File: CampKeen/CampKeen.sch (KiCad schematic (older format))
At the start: 192 parts, among them IC1 LM2597MX-ADJ_NOPB, IC2 LM2670SX-5.0_NOPB, IC3 DS3231SN#, IC4 TL071CP, J1 Vin, J2 CAC, J3 VAC, J4 Screw_Terminal_01x04, J5 GenEnclosure, J6 GenHeadL, J7 GenHeadR, K1 DIP05-1A72-12L, K2 DIP05-1A72-12L, K3 DIP05-1A72-12L, K4 DIP05-1A72-12L, P1 Power, P10 CONN_01X01, P11 CONN_01X01, P12 CONN_01X01, P13 CONN_01X01, P2 Analog, P3 Analog, P4 Digital, P5 PWM, P6 PWM, P7 Communication, P8 CONN_01X01, P9 CONN_01X01, Q1 BC547, Q10 2N7000, Q11 2N7000, Q12 2N7000, Q13 2N7000, Q14 2N7000, Q15 IRF510, Q16 2N7000, Q17 IRF510, Q18 2N7000, Q19 IRF510, Q2 2N7000, Q20 2N7000, Q21 IRF510, Q22 BC547, Q23 2N7000, Q24 IRF510, Q25 2N7000, Q26 2N7000, Q27 IRF510, Q28 2N7000, Q29 IRF510, Q3 2N7000, Q30 2N7000, Q31 IRF510, Q32 BC547, Q33 2N7000, Q35 2N7000, Q36 IRF510, Q37 2N7000, Q38 IRF510, Q39 IRF510, Q4 2N7000, Q40 IRF9Z34NPBF, Q5 2N7000, Q6 BC547, Q7 2N7000, Q8 2N7000, Q9 2N7000, T1 F24-045-C2, U2 MAX232

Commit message: working on the PCB for 0.3
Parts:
- removed IC4: TL071CP, SamacSys_Parts:DIP794W53P254L959H508Q8N, symbol SamacSys_Parts:TL071CP
- removed RV1: 500K, Potentiometer_THT:Potentiometer_Bourns_3296W_Vertical, symbol Device:R_POT_US
- added IC4: INA849DR, SamacSys_Parts:SOIC127P600X175-8N, symbol SamacSys_Parts:INA849DR
- added IC5: LM2904N_NOPB, SamacSys_Parts:DIP794W53P254L959H508Q8N, symbol SamacSys_Parts:LM2904N_NOPB
- added R82: 20K, Resistor_THT:R_Axial_DIN0207_L6.3mm_D2.5mm_P2.54mm_Vertical, symbol Device:R
- added U1: TL431LP, Package_TO_SOT_THT:TO-92_Inline, symbol Reference_Voltage:TL431LP
- R25: footprint Resistor_THT:R_Axial_DIN0207_L6.3mm_D2.5mm_P2.54mm_Vertical -> Resistor_THT:R_Axial_DIN0207_L6.3mm_D2.5mm_P10.16mm_Horizontal
- R29: value 100k -> 1K
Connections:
- net +5V: now also IC4.8 (+VS), IC5.8 (V+)
- net A0: now also IC5.6 (INVERTING_INPUT_B), IC5.7 (OUTPUT_B)
- net A12: now also IC4.7 (OUT); no longer C11.1, J2.2 (Pin_2), R25.1, R29.1, R90.2
- net GND: now also IC4.5 (-VS), IC5.4 (GND), R82.1, U1.2 (A); no longer C11.2
- net at R28.1: now also IC5.5 (NON-INVERTING_INPUT_B), R82.2
- net at T1.5 (12V_@_0.045A_1): now also BR1.3 (~_1); no longer BR1.4 (~_2)
- net at T1.6 (12V_@_0.045A_2): now also BR1.4 (~_2); no longer BR1.3 (~_1)
- net at J2.1 (Pin_1), R25.2: now also C11.1, IC4.1 (-IN)
- new net: IC5.3 (NON-INVERTING_INPUT_A), R29.1, U1.1 (REF), U1.3 (K)
- new net: C11.2, IC4.4 (+IN), J2.2 (Pin_2), R25.1
- new net: IC4.6 (REF), IC5.1 (OUTPUT_A), IC5.2 (INVERTING_INPUT_A), R90.2
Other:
- moved on the sheet: C11, J2, R25, R28, R29, R35, R90

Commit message: 0.3 fixing a bug found in 0.2 hardware.
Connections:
- net +5V: now also K1.2 (COIL_1), K2.2 (COIL_1); no longer Q1.1 (C), Q32.1 (C), Q6.1 (C)
- net GND: now also Q1.3 (E), Q32.3 (E), Q6.3 (E); no longer K1.6 (COIL_2), K2.6 (COIL_2)
- net at O1.11: now also Q32.1 (C); no longer Q32.3 (E)
- new net: K1.6 (COIL_2), Q1.1 (C)
- new net: K2.6 (COIL_2), Q6.1 (C)
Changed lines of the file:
@@
 L power:GND #PWR049
 U 1 1 612DE713
-P 15100 4300
-F 0 "#PWR049" H 15100 4050 50  0001 C CNN
-F 1 "GND" H 15105 4127 50  0000 C CNN
-F 2 "" H 15100 4300 50  0001 C CNN
-F 3 "" H 15100 4300 50  0001 C CNN
-	1    15100 4300
+P 16200 5850
+F 0 "#PWR049" H 16200 5600 50  0001 C CNN
+F 1 "GND" H 16205 5677 50  0000 C CNN
+F 2 "" H 16200 5850 50  0001 C CNN
+F 3 "" H 16200 5850 50  0001 C CNN
+	1    16200 5850
 	1    0    0    -1
 $EndComp
 Wire Wire Line
-	15350 4100 15100 4100
-Wire Wire Line
-	15100 4100 15100 4300
-Wire Wire Line
 	15350 4200 15350 4400
 Wire Wire Line
@@
 	1    0    0    -1
 $EndComp
-Wire Wire Line
-	8350 3950 8350 4050
-Wire Wire Line
-	8350 4050 8900 4050
-Wire Wire Line
-	8350 3550 8350 3300
 $Comp
 L power:+5V #PWR029
 U 1 1 621E716D
-P 8350 3300
-F 0 "#PWR029" H 8350 3150 50  0001 C CNN
-F 1 "+5V" H 8365 3473 50  0000 C CNN
-F 2 "" H 8350 3300 50  0001 C CNN
-F 3 "" H 8350 3300 50  0001 C CNN
-	1    8350 3300
+P 8800 3400
+F 0 "#PWR029" H 8800 3250 50  0001 C CNN
+F 1 "+5V" H 8815 3573 50  0000 C CNN
+F 2 "" H 8800 3400 50  0001 C CNN
+F 3 "" H 8800 3400 50  0001 C CNN
+	1    8800 3400
 	1    0    0    -1
 $EndComp
@@
 	0    1    1    0
 $EndComp
-Wire Wire Line
-	8900 4150 8650 4150
 $Comp
 L power:GND #PWR031
 U 1 1 61234D77
-P 8650 4350
-F 0 "#PWR031" H 8650 4100 50  0001 C CNN
-F 1 "GND" H 8655 4177 50  0000 C CNN
-F 2 "" H 8650 4350 50  0001 C CNN
-F 3 "" H 8650 4350 50  0001 C CNN
-	1    8650 4350
+P 8350 4150
+F 0 "#PWR031" H 8350 3900 50  0001 C CNN
+F 1 "GND" H 8355 3977 50  0000 C CNN
+F 2 "" H 8350 4150 50  0001 C CNN
+F 3 "" H 8350 4150 50  0001 C CNN
+	1    8350 4150
 	1    0    0    -1
 $EndComp
@@
 	0    1    1    0
 $EndComp
-$Comp
-L power:+5V #PWR051
-U 1 1 6236099A
-P 15850 5100
-F 0 "#PWR051" H 15850 4950 50  0001 C CNN
-F 1 "+5V" H 15865 5273 50  0000 C CNN
-F 2 "" H 15850 5100 50  0001 C CNN
-F 3 "" H 15850 5100 50  0001 C CNN
-	1    15850 5100
-	1    0    0    -1
-$EndComp
-Wire Wire Line
-	15850 5350 15850 5100
 Wire Wire Line
 	15850 5750 15850 5850
@@
 Wire Wire Line
 	15850 5850 16200 5850
-Wire Wire Line
-	16200 5850 16200 4700
-Wire Wire Line
-	16200 4700 15200 4700
-Wire Wire Line
-	15200 4700 15200 4000
-Wire Wire Line
-	15200 4000 15350 4000
 $Comp
 L Transistor_FET:2N7000 Q2
@@
 Wire Wire Line
 	20100 22750 20250 22750
-Wire Wire Line
-	8650 4150 8650 4350
 $Comp
 L power:GND #PWR028
@@
 	32400 9000 32400 8000
 Wire Wire Line
-	36350 9000 32400 9000
-Wire Wire Line
-	36350 10500 36350 9000
-Wire Wire Line
 	32300 8100 32150 8100
 Wire Wire Line
@@
 LCDBacklightOut
 Wire Wire Line
-	35500 10500 36350 10500
-Wire Wire Line
 	35500 10000 35500 10500
 Wire Wire Line
@@
 $EndComp
 $Comp
-L power:+5V #PWR0130
-U 1 1 6262263F
-P 35500 9350
-F 0 "#PWR0130" H 35500 9200 50  0001 C CNN
-F 1 "+5V" H 35515 9523 50  0000 C CNN
-F 2 "" H 35500 9350 50  0001 C CNN
-F 3 "" H 35500 9350 50  0001 C CNN
-	1    35500 9350
-	1    0    0    -1
-$EndComp
-Wire Wire Line
-	35500 9600 35500 9350
-$Comp
 L Transistor_BJT:BC547 Q32
 U 1 1 62622636
@@
 Wire Wire Line
 	19500 23700 20050 23700
+Connection ~ 20050 23700
+Wire Wire Line
+	20050 23700 20050 23650
+Wire Wire Line
+	8350 4150 8350 3950
+Wire Wire Line
+	8350 3550 8550 3550
+Wire Wire Line
+	8550 3550 8550 4150
+Wire Wire Line
+	8550 4150 8900 4150
+Wire Wire Line
+	8900 4050 8800 4050
+Wire Wire Line
+	8800 3400 8800 4050
+$Comp
+L power:+5V #PWR051
+U 1 1 6236099A
+P 15150 3750
+F 0 "#PWR051" H 15150 3600 50  0001 C CNN
+F 1 "+5V" H 15165 3923 50  0000 C CNN
+F 2 "" H 15150 3750 50  0001 C CNN
+F 3 "" H 15150 3750 50  0001 C CNN
+	1    15150 3750
+	1    0    0    -1
+$EndComp
+Wire Wire Line
+	15150 4000 15150 3750
+Wire Wire Line
+	15150 4000 15350 4000
+Wire Wire Line
+	15850 5350 15850 4700
+Wire Wire Line
+	15850 4700 15150 4700
+Wire Wire Line
+	15150 4700 15150 4100
+Wire Wire Line
+	15150 4100 15350 4100
+$Comp
+L power:GND #PWR?
+U 1 1 62559C03
+P 35500 10500
+F 0 "#PWR?" H 35500 10250 50  0001 C CNN
+F 1 "GND" H 35505 10327 50  0000 C CNN
+F 2 "" H 35500 10500 50  0001 C CNN
+F 3 "" H 35500 10500 50  0001 C CNN
+	1    35500 10500
+	1    0    0    -1
+$EndComp
+Wire Wire Line
+	35500 9600 35500 9000
+Wire Wire Line
+	35500 9000 32400 9000
 Wire Bus Line
 	8600 7000 25650 7000
@@
 Wire Bus Line
 	21850 16650 25650 16650
-Connection ~ 20050 23700
-Wire Wire Line
-	20050 23700 20050 23650
 $EndSCHEMATC

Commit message: before removing my homegrown AC monitoring stuff.
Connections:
- net +5V: now also K4.2 (COIL_1); no longer Q22.1 (C)
- net GND: now also Q22.3 (E); no longer K4.6 (COIL_2)
- new net: K4.6 (COIL_2), Q22.1 (C)
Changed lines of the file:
@@
 	1    0    0    -1
 $EndComp
-Wire Wire Line
-	30500 16950 30500 17050
-Wire Wire Line
-	30500 17050 31050 17050
-Wire Wire Line
-	30500 16550 30500 16300
 $Comp
 L power:+5V #PWR0110
 U 1 1 621F0FD9
-P 30500 16300
-F 0 "#PWR0110" H 30500 16150 50  0001 C CNN
-F 1 "+5V" H 30515 16473 50  0000 C CNN
-F 2 "" H 30500 16300 50  0001 C CNN
-F 3 "" H 30500 16300 50  0001 C CNN
-	1    30500 16300
+P 30850 16350
+F 0 "#PWR0110" H 30850 16200 50  0001 C CNN
+F 1 "+5V" H 30865 16523 50  0000 C CNN
+F 2 "" H 30850 16350 50  0001 C CNN
+F 3 "" H 30850 16350 50  0001 C CNN
+	1    30850 16350
 	1    0    0    -1
 $EndComp
@@
 	0    1    1    0
 $EndComp
-Wire Wire Line
-	31050 17150 30800 17150
 $Comp
 L power:GND #PWR0115
 U 1 1 621F0FE6
-P 30800 17350
-F 0 "#PWR0115" H 30800 17100 50  0001 C CNN
-F 1 "GND" H 30805 17177 50  0000 C CNN
-F 2 "" H 30800 17350 50  0001 C CNN
-F 3 "" H 30800 17350 50  0001 C CNN
-	1    30800 17350
+P 30500 17250
+F 0 "#PWR0115" H 30500 17000 50  0001 C CNN
+F 1 "GND" H 30505 17077 50  0000 C CNN
+F 2 "" H 30500 17250 50  0001 C CNN
+F 3 "" H 30500 17250 50  0001 C CNN
+	1    30500 17250
 	1    0    0    -1
 $EndComp
-Wire Wire Line
-	30800 17150 30800 17350
 $Comp
 L power:GND #PWR0109
@@
 	12100 14800 12100 14700
 Connection ~ 12100 14600
-Connection ~ 12100 14800
 Wire Wire Line
 	12600 14700 12100 14700
@@
 	12100 14700 12100 14600
 Wire Wire Line
-	12600 14900 12100 14900
-Wire Wire Line
-	12100 14900 12100 14800
-Wire Wire Line
 	13900 15100 13500 15100
 Wire Wire Line
@@
 	15150 4100 15350 4100
 $Comp
-L power:GND #PWR?
+L power:GND #PWR0130
 U 1 1 62559C03
 P 35500 10500
-F 0 "#PWR?" H 35500 10250 50  0001 C CNN
+F 0 "#PWR0130" H 35500 10250 50  0001 C CNN
 F 1 "GND" H 35505 10327 50  0000 C CNN
 F 2 "" H 35500 10500 50  0001 C CNN
@@
 Wire Wire Line
 	35500 9000 32400 9000
+Wire Wire Line
+	30500 16950 30500 17250
+Wire Wire Line
+	31050 17050 30850 17050
+Wire Wire Line
+	30850 17050 30850 16350
+Wire Wire Line
+	30500 16550 30800 16550
+Wire Wire Line
+	30800 16550 30800 17150
+Wire Wire Line
+	30800 17150 31050 17150
 Wire Bus Line
-	8600 7000 25650 7000
+	25650 12850 40250 12850
+Wire Bus Line
+	25650 7000 42500 7000
 Wire Bus Line
 	36400 16150 36400 18600
@@
 	21650 18600 36400 18600
 Wire Bus Line
-	25650 7000 42500 7000
-Wire Bus Line
-	25650 12850 40250 12850
-Wire Bus Line
 	25650 12850 25650 16650
 Wire Bus Line
 	21850 16650 25650 16650
+Wire Bus Line
+	8600 7000 25650 7000
+Connection ~ 12100 14800
+Wire Wire Line
+	12100 14900 12100 14800
+Wire Wire Line
+	12600 14900 12100 14900
 $EndSCHEMATC

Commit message: files submitted for Fab Verions 0.5
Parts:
- removed BR1: DF04M, SamacSys_Parts:DIP825W58P510L828H330Q4N, symbol SamacSys_Parts:DF04M
- removed C11: 10uF, Capacitor_THT:C_Rect_L9.0mm_W3.6mm_P7.50mm_MKT, symbol Device:C
- removed C12: 2.2uF, Capacitor_THT:CP_Radial_D4.0mm_P2.00mm, symbol Device:CP
- removed C13: 10nF, Capacitor_THT:C_Disc_D7.5mm_W5.0mm_P5.00mm, symbol Device:C
- removed IC4: INA849DR, SamacSys_Parts:SOIC127P600X175-8N, symbol SamacSys_Parts:INA849DR
- removed IC5: LM2904N_NOPB, SamacSys_Parts:DIP794W53P254L959H508Q8N, symbol SamacSys_Parts:LM2904N_NOPB
- removed J2: CAC, TerminalBlock_Phoenix:TerminalBlock_Phoenix_MKDS-1,5-2-5.08_1x02_P5.08mm_Horizontal, symbol Connector:Screw_Terminal_01x02
- removed K3: DIP05-1A72-12L, SamacSys_Parts:DIP051A7212L, symbol SamacSys_Parts:DIP05-1A72-12L
- removed R25: 33, Resistor_THT:R_Axial_DIN0207_L6.3mm_D2.5mm_P10.16mm_Horizontal, symbol Device:R
- removed R29: 1K, Resistor_THT:R_Axial_DIN0207_L6.3mm_D2.5mm_P2.54mm_Vertical, symbol Device:R
- removed R30: 1M, Resistor_THT:R_Axial_DIN0207_L6.3mm_D2.5mm_P2.54mm_Vertical, symbol Device:R
- removed R36: 180k, Resistor_THT:R_Axial_DIN0207_L6.3mm_D2.5mm_P2.54mm_Vertical, symbol Device:R
- removed R90: 100k, Resistor_THT:R_Axial_DIN0207_L6.3mm_D2.5mm_P2.54mm_Vertical, symbol Device:R
- removed T1: F24-045-C2, SamacSys_Parts:F24045C2, symbol SamacSys_Parts:F24-045-C2
- removed U1: TL431LP, Package_TO_SOT_THT:TO-92_Inline, symbol Reference_Voltage:TL431LP
- removed VACFuse1: VAC, SamacSys_Parts:BK_HTC-15M, symbol SamacSys_Parts:BK_HTC-15M
- added IC4: CD74HC4050ME4, SOIC127P600X175-16N, symbol SamacSys_Parts:CD74HC4050ME4
- added IC5: TL071CP, DIP794W53P254L959H508Q8N, symbol SamacSys_Parts:TL071CP
- added J2: CircuitSetupsSplitPhase, Connector_PinSocket_2.54mm:PinSocket_1x09_P2.54mm_Vertical, symbol Connector_Generic:Conn_01x09
- J3: value VAC -> Vin
- R2, R3: footprint Resistor_THT:R_Axial_DIN0207_L6.3mm_D2.5mm_P2.54mm_Vertical -> Resistor_THT:R_Axial_DIN0204_L3.6mm_D1.6mm_P7.62mm_Horizontal
- R82: value 20K -> 19.2K
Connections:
- net +12V: now also J3.1 (Pin_1)
- net +3V3: now also IC4.1 (VCC)
- net +5V: now also IC5.7 (VCC+)
- net 41: now also IC4.14 (6A); no longer Q35.1 (S), R83.1
- net 50(MISO): now also IC4.4 (2Y), IC4.5 (2A), J2.4 (Pin_4)
- net 51(MOSI): now also IC4.6 (3Y), IC4.7 (3A), J2.3 (Pin_3)
- net 52(SCK): now also IC4.3 (1A)
- net A0: now also IC5.2 (IN-), IC5.6 (OUT)
- net A11: no longer P3.4 (Pin_4)
- net A12: no longer P3.5 (Pin_5)
- net GND: now also J3.2 (Pin_2), IC4.8 (GND), IC5.4 (VCC-), J2.1 (Pin_1)
- net at R28.1, R82.2: now also IC5.3 (IN+)
- new net: Q35.1 (S), R83.1
- new net CS: IC4.15 (6Y), J2.6 (Pin_6)
- new net SCLK: IC4.2 (1Y), J2.5 (Pin_5)
- no-connect marks 36 -> 42
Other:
- moved on the sheet: C1, C10, C18, C2, C3, C4, C6, C7, C8, C9, D1, D2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

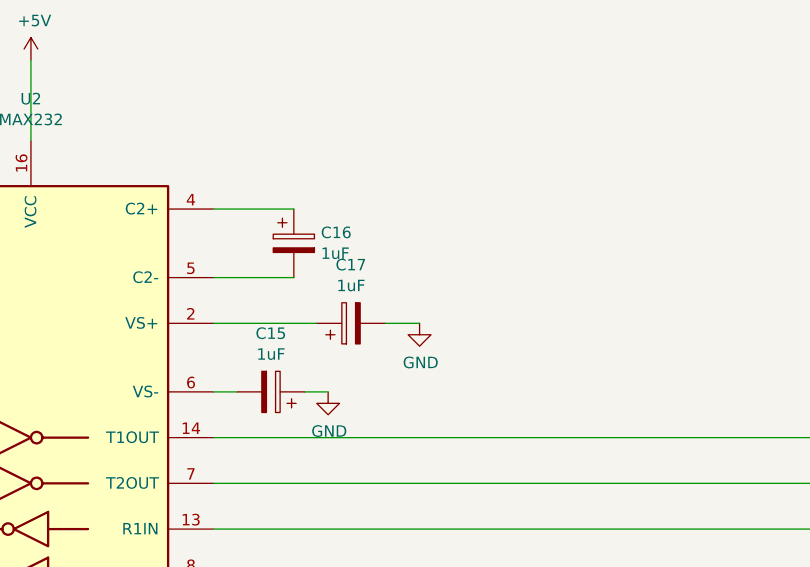
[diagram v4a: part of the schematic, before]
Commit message: fixed the mistake on the RS232 driver.
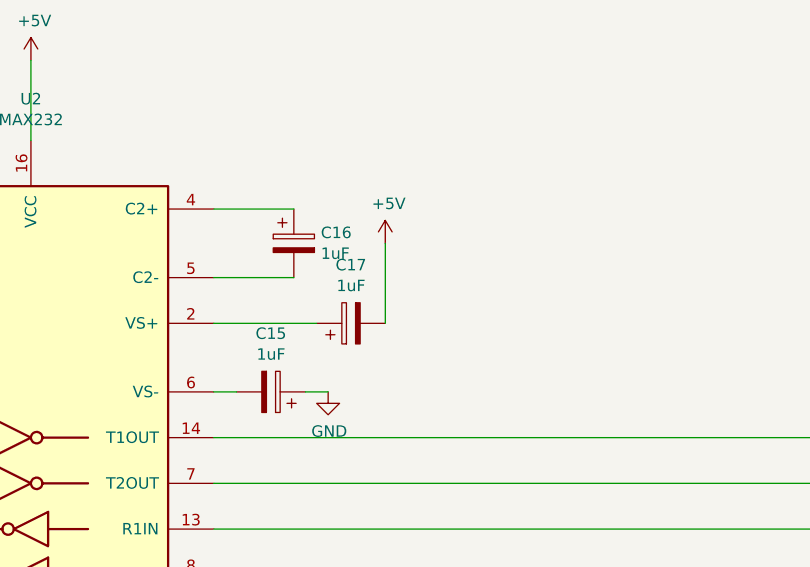
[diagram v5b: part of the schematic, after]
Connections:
- net +5V: now also C17.2
- net GND: no longer C17.2
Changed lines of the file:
@@
 	1    0    0    -1
 $EndComp
-$Comp
-L power:GND #PWR0108
-U 1 1 61FF6266
-P 29800 14900
-F 0 "#PWR0108" H 29800 14650 50  0001 C CNN
-F 1 "GND" H 29805 14727 50  0000 C CNN
-F 2 "" H 29800 14900 50  0001 C CNN
-F 3 "" H 29800 14900 50  0001 C CNN
-	1    29800 14900
-	1    0    0    -1
-$EndComp
 Wire Wire Line
 	29400 15200 29300 15200
 Wire Wire Line
-	29650 14900 29800 14900
-Wire Wire Line
 	27300 15600 27150 15600
 Wire Wire Line
@@
 NoConn ~ 21100 20750
 NoConn ~ 21100 20650
+Wire Wire Line
+	29650 14900 29650 14550
+$Comp
+L power:+5V #PWR?
+U 1 1 61822607
+P 29650 14550
+F 0 "#PWR?" H 29650 14400 50  0001 C CNN
+F 1 "+5V" H 29665 14723 50  0000 C CNN
+F 2 "" H 29650 14550 50  0001 C CNN
+F 3 "" H 29650 14550 50  0001 C CNN
+	1    29650 14550
+	1    0    0    -1
+$EndComp
 Wire Bus Line
 	18950 18600 18950 21000

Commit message: adding docs and cleaning up pin mappings and extra parts for ports.
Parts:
- removed Q35: 2N7000, Package_TO_SOT_THT:TO-92_Inline, symbol Transistor_FET:2N7000
- removed R81, R83: 1M, Resistor_THT:R_Axial_DIN0207_L6.3mm_D2.5mm_P2.54mm_Vertical, symbol Device:R
- renumbered Tanks2 to Tanks0
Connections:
- net +5V: no longer Temps1.4
- net A11: now also P3.4 (Pin_4)
- net A12: now also P3.5 (Pin_5)
- no-connect marks 42 -> 44
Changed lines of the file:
@@
 $EndComp
 $Comp
-L Transistor_FET:2N7000 Q35
-U 1 1 6240292F
-P 37100 3900
-F 0 "Q35" H 37304 3946 50  0000 L CNN
-F 1 "2N7000" H 37304 3855 50  0000 L CNN
-F 2 "Package_TO_SOT_THT:TO-92_Inline" H 37300 3825 50  0001 L CIN
-F 3 "https://www.onsemi.com/pub/Collateral/NDS7002A-D.PDF" H 37100 3900 50  0001 L CNN
-	1    37100 3900
-	1    0    0    -1
-$EndComp
-Wire Wire Line
-	37200 3700 37200 3550
-$Comp
-L power:+5V #PWR0134
-U 1 1 62402936
-P 37200 3550
-F 0 "#PWR0134" H 37200 3400 50  0001 C CNN
-F 1 "+5V" H 37215 3723 50  0000 C CNN
-F 2 "" H 37200 3550 50  0001 C CNN
-F 3 "" H 37200 3550 50  0001 C CNN
-	1    37200 3550
-	1    0    0    -1
-$EndComp
-Wire Wire Line
-	37200 4200 37200 4150
-Connection ~ 37200 4650
-Wire Wire Line
-	37200 4650 37200 4500
-Wire Wire Line
-	36650 3900 36900 3900
-Wire Wire Line
-	36650 4200 36650 3900
-$Comp
-L Device:R R83
-U 1 1 62402941
-P 37200 4350
-F 0 "R83" H 37270 4396 50  0000 L CNN
-F 1 "1M" H 37270 4305 50  0000 L CNN
-F 2 "Resistor_THT:R_Axial_DIN0207_L6.3mm_D2.5mm_P2.54mm_Vertical" V 37130 4350 50  0001 C CNN
-F 3 "~" H 37200 4350 50  0001 C CNN
-	1    37200 4350
-	1    0    0    -1
-$EndComp
-Wire Wire Line
-	36650 4650 37200 4650
-Wire Wire Line
-	36650 4500 36650 4650
-$Comp
-L power:GND #PWR0135
-U 1 1 62402949
-P 37200 4650
-F 0 "#PWR0135" H 37200 4400 50  0001 C CNN
-F 1 "GND" H 37205 4477 50  0000 C CNN
-F 2 "" H 37200 4650 50  0001 C CNN
-F 3 "" H 37200 4650 50  0001 C CNN
-	1    37200 4650
-	1    0    0    -1
-$EndComp
-$Comp
-L Device:R R81
-U 1 1 6240294F
-P 36650 4350
-F 0 "R81" H 36720 4396 50  0000 L CNN
-F 1 "1M" H 36720 4305 50  0000 L CNN
-F 2 "Resistor_THT:R_Axial_DIN0207_L6.3mm_D2.5mm_P2.54mm_Vertical" V 36580 4350 50  0001 C CNN
-F 3 "~" H 36650 4350 50  0001 C CNN
-	1    36650 4350
-	1    0    0    -1
-$EndComp
-Connection ~ 37200 4150
-Wire Wire Line
-	37200 4150 37200 4100
-$Comp
 L Transistor_FET:2N7000 Q28
 U 1 1 625DCC2A
@@
 Entry Wire Line
 	35800 7000 35700 6900
-Entry Wire Line
-	36600 7000 36500 6900
 Text Label 22050 16550 1    50   ~ 0
 A15
@@
 	14700 2450 14700 3050
 $Comp
-L SamacSys_Parts:1727751 Tanks2
+L SamacSys_Parts:1727751 Tanks0
 U 1 1 61280B03
 P 15000 2050
-F 0 "Tanks2" H 15450 2315 50  0000 C CNN
+F 0 "Tanks0" H 15450 2315 50  0000 C CNN
 F 1 "Tanks" H 15450 2224 50  0000 C CNN
 F 2 "SamacSys_Parts:1727751" H 15750 2150 50  0001 L CNN
@@
 	36000 4150 36350 4150
 Wire Wire Line
-	36500 5000 37650 5000
-Wire Wire Line
-	37650 5000 37650 4150
-Wire Wire Line
-	37200 4150 37650 4150
-Wire Wire Line
-	36500 5000 36500 6900
-Wire Wire Line
 	31100 3850 31100 2050
 Wire Wire Line
@@
 Connection ~ 34200 3850
 Wire Wire Line
-	36650 3900 36650 2850
-Wire Wire Line
-	36650 2850 44650 2850
-Wire Wire Line
-	44650 2850 44650 15700
-Wire Wire Line
-	44650 15700 33450 15700
-Connection ~ 36650 3900
-Wire Wire Line
 	33450 15600 44600 15600
 Wire Wire Line
@@
 Wire Wire Line
 	30850 17050 30850 16350
-Connection ~ 12100 14800
-Wire Wire Line
-	12100 14900 12100 14800
-Wire Wire Line
-	12600 14900 12100 14900
 $Comp
 L Connector_Generic:Conn_01x09 J2
@@
 	29650 14900 29650 14550
 $Comp
-L power:+5V #PWR?
+L power:+5V #PWR0108
 U 1 1 61822607
 P 29650 14550
-F 0 "#PWR?" H 29650 14400 50  0001 C CNN
+F 0 "#PWR0108" H 29650 14400 50  0001 C CNN
 F 1 "+5V" H 29665 14723 50  0000 C CNN
 F 2 "" H 29650 14550 50  0001 C CNN
@@
 	1    0    0    -1
 $EndComp
+Wire Wire Line
+	22050 16050 21600 16050
+Wire Wire Line
+	21600 16150 22050 16150
+NoConn ~ 21600 16050
+NoConn ~ 21600 16150
 Wire Bus Line
 	18950 18600 18950 21000
 Wire Bus Line
+	25650 7000 42500 7000
+Wire Bus Line
 	8600 7000 25650 7000
 Wire Bus Line
@@
 	18950 18600 36400 18600
 Wire Bus Line
-	25650 7000 42500 7000
-Wire Bus Line
 	25650 12850 40250 12850

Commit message: continue on fixing and adding stuff. fixed the fuck up on the schematic for the 5to3 volt converter. changing out the voltage sensor to a opa2340, ading asecond general voltage sensor. and an additional NTC sensor. RTC Battery monitor.
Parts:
- removed IC5: TL071CP, DIP794W53P254L959H508Q8N, symbol SamacSys_Parts:TL071CP
- added IC5: OPA2340PA, DIP794W53P254L959H508Q8N, symbol SamacSys_Parts:OPA2340PA
- added J8: Conn_01x02, Connector_PinHeader_2.54mm:PinHeader_1x02_P2.54mm_Vertical, symbol Connector_Generic:Conn_01x02
- added R25: 10k, Resistor_THT:R_Axial_DIN0207_L6.3mm_D2.5mm_P2.54mm_Vertical, symbol Device:R
- added R29: 47K, Resistor_THT:R_Axial_DIN0207_L6.3mm_D2.5mm_P2.54mm_Vertical, symbol Device:R
- added RV1: R_POT_US, Potentiometer_THT:Potentiometer_Bourns_3296W_Vertical, symbol Device:R_POT_US
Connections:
- net +5V: now also IC5.8 (V+)
- net 50(MISO): no longer IC4.5 (2A), J2.4 (Pin_4)
- net 51(MOSI): no longer IC4.6 (3Y), J2.3 (Pin_3)
- net A0: now also IC5.1 (OUTA), IC5.2 (-INA)
- net A11: now also Temps1.4, R25.2
- net A12: now also IC5.6 (-INB), IC5.7 (OUTB), R29.2
- net A14: now also IC3.14 (VBAT), RTCBattery1.1 (+); no longer Tanks0.11
- net A15: no longer Tanks0.12
- net GND: now also IC5.4 (V-), R25.1, R29.1, RV1.3
- net at R28.1, R82.2: now also IC5.3 (+INA)
- net AUXVoltage: now reaches IO1.10
- net AUXVoltage: now also RV1.1
- net CS renamed 3.3CS
- net SCLK renamed 3.3SCLK
- new net: IC5.5 (+INB), J8.1 (Pin_1)
- new net: J8.2 (Pin_2), RV1.2
- new net 3.3MISO: IC4.5 (2A), J2.4 (Pin_4)
- new net 3.3MOSI: IC4.6 (3Y), J2.3 (Pin_3)
- no-connect marks 44 -> 40
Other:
- moved on the sheet: J3, R28, R35, R82
